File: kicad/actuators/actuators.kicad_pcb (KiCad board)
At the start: 2 copper layers, 47 parts, among them J1 Conn_01x06, J2 Conn_01x06, J3 Conn_01x06, J4 Conn_01x06, U1 DRV8874PWPR, U2 DRV8874PWPR, U3 DRV8874PWPR, U4 DRV8874PWPR, U6 STM32G431R6Tx

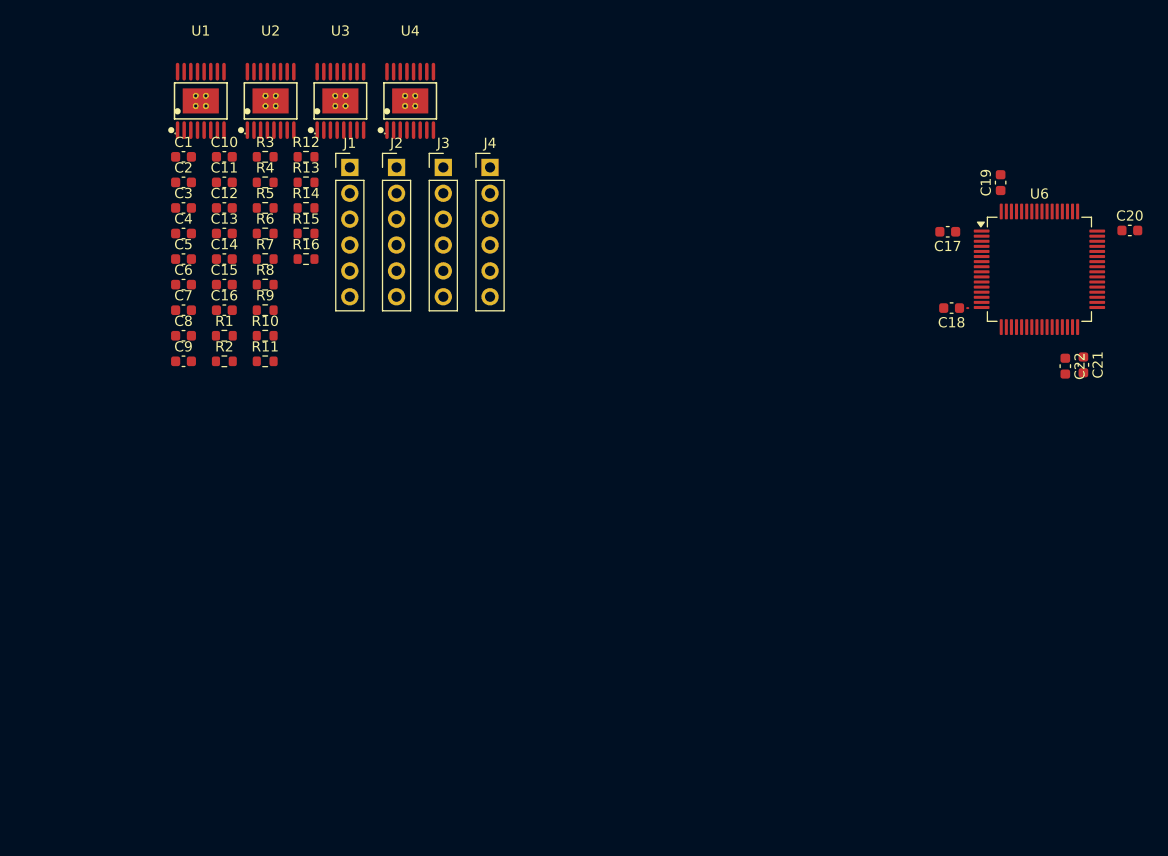
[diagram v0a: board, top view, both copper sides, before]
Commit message: completed the actuator pcb
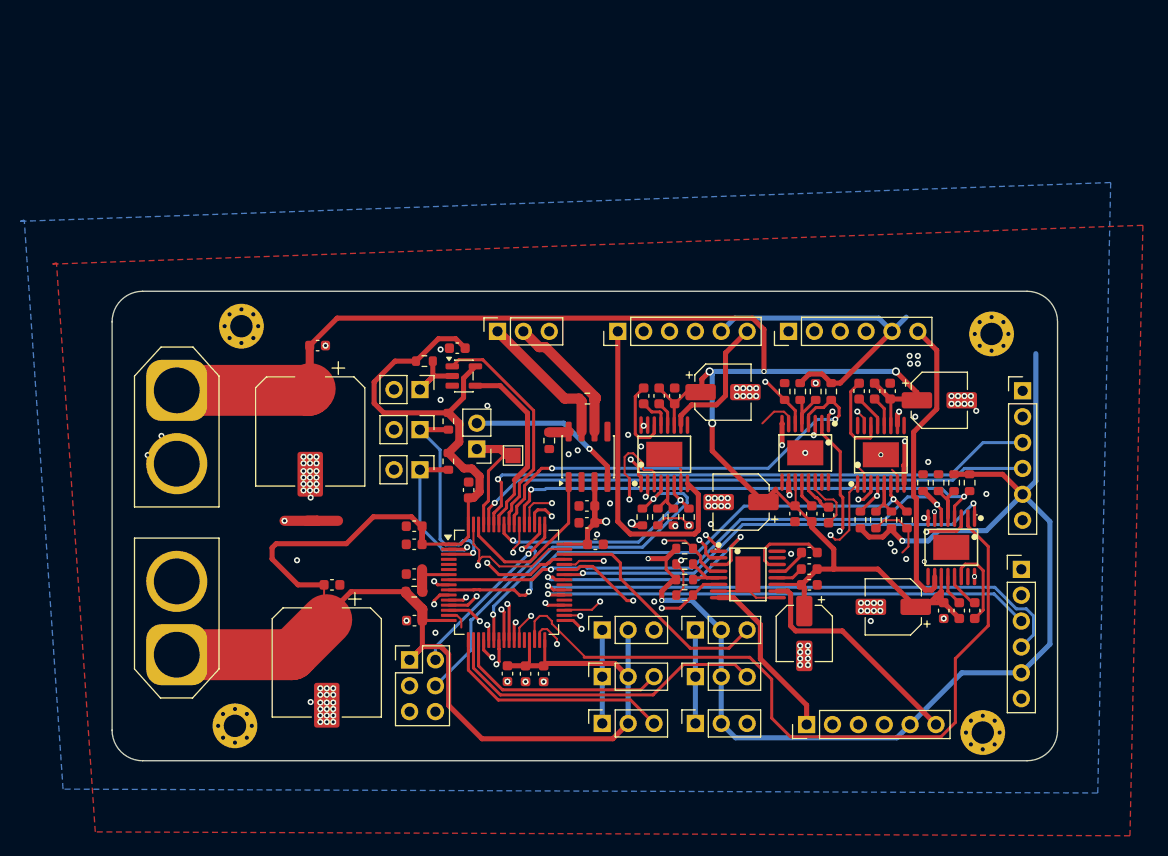
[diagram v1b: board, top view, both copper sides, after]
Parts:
- added C23: 22nF, Capacitor_SMD:C_0603_1608Metric, F.Cu at (161.6, 118.0)
- added C24: 100nf, Capacitor_SMD:C_0603_1608Metric, F.Cu at (163.1, 118.0)
- added C25: 0.1uF, Capacitor_SMD:C_0603_1608Metric, F.Cu at (169.9, 139.6)
- added C26: 100nf, Capacitor_SMD:C_0603_1608Metric, F.Cu at (164.7, 118.0)
- added C27: 22uF, Capacitor_SMD:CP_Elec_5x5.3, F.Cu at (165.0, 139.2)
- added C28: 22uF, Capacitor_SMD:CP_Elec_5x5.3, F.Cu at (169.5, 118.9)
- added C29: 22nF, Capacitor_SMD:C_0603_1608Metric, F.Cu at (156.7, 133.9)
- added C30: 100nf, Capacitor_SMD:C_0603_1608Metric, F.Cu at (156.7, 135.5)
- added C31: 22nF, Capacitor_SMD:C_0603_1608Metric, F.Cu at (158.6, 130.2)
- added C32: 100nf, Capacitor_SMD:C_0603_1608Metric, F.Cu at (157.0, 130.0)
- added C33: 0.1uF, Capacitor_SMD:C_0603_1608Metric, F.Cu at (156.7, 137.0)
- added C34: 0.1uF, Capacitor_SMD:C_0603_1608Metric, F.Cu at (155.3, 130.0)
- added C35: 22uF, Capacitor_SMD:CP_Elec_5x5.3, F.Cu at (156.2, 141.8)
- added C36: 22uF, Capacitor_SMD:CP_Elec_5x5.3, F.Cu at (150.0, 128.9)
- added J10: Conn_01x03, Connector_PinSocket_2.54mm:PinSocket_1x03_P2.54mm_Vertical, F.Cu at (136.4, 146.1)
- added J11: Conn_01x03, Connector_PinSocket_2.54mm:PinSocket_1x03_P2.54mm_Vertical, F.Cu at (136.4, 141.5)
- added J12: Conn_01x03, Connector_PinSocket_2.54mm:PinSocket_1x03_P2.54mm_Vertical, F.Cu at (126.1, 112.1)
- added J13: ESTOP SWITCH, Connector_PinHeader_2.54mm:PinHeader_1x02_P2.54mm_Vertical, F.Cu at (118.5, 117.9)
- added J14: Conn_01x06, Connector_PinHeader_2.54mm:PinHeader_1x06_P2.54mm_Vertical, F.Cu at (154.7, 112.1)
- added J15: Conn_01x06, Connector_PinHeader_2.54mm:PinHeader_1x06_P2.54mm_Vertical, F.Cu at (177.7, 118.0)
- added J16: LIMIT-SWITCH, Connector_PinHeader_2.54mm:PinHeader_1x02_P2.54mm_Vertical, F.Cu at (118.5, 125.7)
- added J17: LIMIT-SWITCH, Connector_PinHeader_2.54mm:PinHeader_1x02_P2.54mm_Vertical, F.Cu at (118.5, 121.8)
- added J18: Conn_01x06, Connector_PinHeader_2.54mm:PinHeader_1x06_P2.54mm_Vertical, F.Cu at (156.5, 150.7)
- added J19: Conn_01x06, Connector_PinHeader_2.54mm:PinHeader_1x06_P2.54mm_Vertical, F.Cu at (177.5, 135.5)
- added J5: Conn_01x06, Connector_PinHeader_2.54mm:PinHeader_1x06_P2.54mm_Vertical, F.Cu at (137.9, 112.1)
- added J6: Conn_01x03, Connector_PinSocket_2.54mm:PinSocket_1x03_P2.54mm_Vertical, F.Cu at (145.5, 150.6)
- added J7: Conn_01x03, Connector_PinSocket_2.54mm:PinSocket_1x03_P2.54mm_Vertical, F.Cu at (145.5, 146.1)
- added J8: Conn_01x03, Connector_PinSocket_2.54mm:PinSocket_1x03_P2.54mm_Vertical, F.Cu at (145.5, 141.5)
- added J9: Conn_01x03, Connector_PinSocket_2.54mm:PinSocket_1x03_P2.54mm_Vertical, F.Cu at (136.4, 150.6)
- added R17: 10k, Resistor_SMD:R_0603_1608Metric, F.Cu at (121.3, 124.9)
- added R18: 3.3k, Resistor_SMD:R_0603_1608Metric, F.Cu at (144.5, 136.5)
- added R19: 10k, Resistor_SMD:R_0603_1608Metric, F.Cu at (144.5, 135.0)
- added R20: 3.3k, Resistor_SMD:R_0603_1608Metric, F.Cu at (155.8, 118.0)
- added R21: 10k, Resistor_SMD:R_0603_1608Metric, F.Cu at (157.4, 118.0)
- added R22: 10k, Resistor_SMD:R_0603_1608Metric, F.Cu at (121.3, 121.0)
- added R23: 10k, Resistor_SMD:R_0603_1608Metric, F.Cu at (144.5, 133.5)
- added R24: 1.8k, Resistor_SMD:R_0603_1608Metric, F.Cu at (144.5, 138.0)
- added R25: 10k, Resistor_SMD:R_0603_1608Metric, F.Cu at (158.9, 118.0)
- added R26: 1.8k, Resistor_SMD:R_0603_1608Metric, F.Cu at (154.3, 118.0)
- added REF**: MountingHole_2.2mm_M2_Pad_Via, MountingHole:MountingHole_2.2mm_M2_Pad_Via, F.Cu at (173.8, 151.5)
- added REF**: MountingHole_2.2mm_M2_Pad_Via, MountingHole:MountingHole_2.2mm_M2_Pad_Via, F.Cu at (174.6, 112.4)
- added REF**: MountingHole_2.2mm_M2_Pad_Via, MountingHole:MountingHole_2.2mm_M2_Pad_Via, F.Cu at (100.3, 150.9)
- added REF**: MountingHole_2.2mm_M2_Pad_Via, MountingHole:MountingHole_2.2mm_M2_Pad_Via, F.Cu at (101.0, 111.6)
- added TP1: Boot, TestPoint:TestPoint_Pad_1.5x1.5mm, F.Cu at (127.6, 124.3)
- added U5: DRV8874PWPR, drv8874:HTSSOP-16_L5.0-W4.4-P0.65-LS6.4-BL-EP, F.Cu at (163.8, 124.3)
- added U7: DRV8874PWPR, drv8874:HTSSOP-16_L5.0-W4.4-P0.65-LS6.4-BL-EP, F.Cu at (150.7, 136.0)
- added U8: DRV8874PWPR, drv8874:HTSSOP-16_L5.0-W4.4-P0.65-LS6.4-BL-EP, F.Cu at (156.3, 124.1)
- C1: value 0.022uF -> 100nF
- C10, C11, C15, C6, C7: value 0.1uF -> 100nf
- C12: value 22uF -> 1uF
- C13: value 0.022uF -> 4.7uF
- C14: value 0.1uF -> 4.7uF
- C16: value 22uF -> 0.022uF
- C17, C18: value C -> 0.1uF
- C19: value C -> 22uF; footprint Capacitor_SMD:C_0603_1608Metric -> Capacitor_SMD:CP_Elec_5x5.3
- C2, C3: value 0.1uF -> 100nF
- C20, C22: value C -> 100nf
- C21: value C -> 22nF
- C4: value 22uF -> 470uf; footprint Capacitor_SMD:C_0603_1608Metric -> Capacitor_SMD:CP_Elec_10x10.5
- C5: value 0.022uF -> 470uf; footprint Capacitor_SMD:C_0603_1608Metric -> Capacitor_SMD:CP_Elec_10x10.5
- C8: value 22uF -> 100nf
- C9: value 0.022uF -> 100nf
- J1: value Conn_01x06 -> 3V3_IN; footprint Connector_PinHeader_2.54mm:PinHeader_1x06_P2.54mm_Vertical -> Connector_AMASS:AMASS_XT60-M_1x02_P7.20mm_Vertical
- J2: value Conn_01x06 -> 6V_IN; footprint Connector_PinHeader_2.54mm:PinHeader_1x06_P2.54mm_Vertical -> Connector_AMASS:AMASS_XT60-M_1x02_P7.20mm_Vertical
- J3: value Conn_01x06 -> Jumper; footprint Connector_PinHeader_2.54mm:PinHeader_1x06_P2.54mm_Vertical -> Connector_PinHeader_2.54mm:PinHeader_1x02_P2.54mm_Vertical
- J4: value Conn_01x06 -> Conn_02x03_Odd_Even; footprint Connector_PinHeader_2.54mm:PinHeader_1x06_P2.54mm_Vertical -> Connector_PinHeader_2.54mm:PinHeader_2x03_P2.54mm_Vertical
- R10: value 10k -> 3.3k
- R12: value 1.8k -> 10k
- R13, R3, R9: value 3.3k -> 10k
- R14: value 10k -> 1.8k
- R2, R8: value 1.8k -> 3.3k
- R5: value 3.3k -> 1.8k
- R7: value 10k -> 120
- U1: value DRV8874PWPR -> STM32G431R6Tx; footprint drv8874:HTSSOP-16_L5.0-W4.4-P0.65-LS6.4-BL-EP -> Package_QFP:LQFP-64_10x10mm_P0.5mm
- U3: value DRV8874PWPR -> SN65HVD230; footprint drv8874:HTSSOP-16_L5.0-W4.4-P0.65-LS6.4-BL-EP -> Package_SO:SOIC-8_3.9x4.9mm_P1.27mm
- U6: value STM32G431R6Tx -> 74LVC1G08; footprint Package_QFP:LQFP-64_10x10mm_P0.5mm -> Package_TO_SOT_SMD:SOT-23-5
- moved R13 71.5 mm to (172.5, 127.0), turned to -90 degrees
- moved R8 70.4 mm to (170.9, 127.0), turned to -90 degrees
- moved U4 68.9 mm to (170.7, 133.3), turned to 180 degrees
- moved R9 68.3 mm to (169.4, 127.0), turned to 90 degrees
- moved C20 67.0 mm to (122.2, 113.8)
- moved R14 66.3 mm to (167.9, 127.0), turned to 90 degrees
- moved R16 64.3 mm to (166.3, 130.7), turned to -90 degrees
- moved R10 64.1 mm to (164.8, 130.7), turned to 90 degrees
- moved R11 62.0 mm to (163.3, 130.7), turned to -90 degrees
- moved R15 61.3 mm to (161.7, 130.7), turned to 90 degrees
- moved U6 57.5 mm to (122.8, 116.5)
- moved U1 56.0 mm to (127.0, 136.8)
- moved R3 52.3 mm to (141.9, 130.4), turned to -90 degrees
- moved U2 51.9 mm to (142.5, 124.2)
- moved R5 51.5 mm to (144.9, 130.4), turned to -90 degrees
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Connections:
- C1 pad 1: Net-(U1-CPL) -> Net-(U1-PG10)
- C1 pad 2: Net-(U1-CPH) -> GND
- C10 pad 1: Net-(U3-VCP) -> +3V3
- C10 pad 2: +6V -> GND
- C11 pad 1: +6V -> +3V3
- C12 pad 1: +6V -> +3V3
- C13 pad 1: Net-(U4-CPL) -> +3V3
- C13 pad 2: Net-(U4-CPH) -> GND
- C14 pad 1: Net-(U4-VCP) -> +3V3
- C14 pad 2: +6V -> GND
- C15 pad 1: +6V -> +3V3
- C16 pad 1: +6V -> Net-(U2-CPL)
- C16 pad 2: GND -> Net-(U2-CPH)
- C17 pad 1: Net-(U6-VBAT) -> Net-(U2-VCP)
- C17 pad 2: GND -> +6V
- C18 pad 1: Net-(U6-VBAT) -> +6V
- C19 pad 1: Net-(U6-VBAT) -> +6V
- C2 pad 1: Net-(U1-VCP) -> +3V3
- C2 pad 2: +6V -> GND
- C20 pad 1: Net-(U6-VBAT) -> GND
- C20 pad 2: GND -> +3V3
- C21 pad 1: Net-(U6-VBAT) -> Net-(U4-CPL)
- C21 pad 2: GND -> Net-(U4-CPH)
- C22 pad 1: Net-(U6-VBAT) -> Net-(U4-VCP)
- C22 pad 2: GND -> +6V
- C4 pad 1: +6V -> +3V3
- C5 pad 1: Net-(U2-CPL) -> +6V
- C5 pad 2: Net-(U2-CPH) -> GND
- C6 pad 1: Net-(U2-VCP) -> +3V3
- C6 pad 2: +6V -> GND
- C7 pad 1: +6V -> +3V3
- C8 pad 1: +6V -> +3V3
- C9 pad 1: Net-(U3-CPL) -> +3V3
- C9 pad 2: Net-(U3-CPH) -> GND
- J1 pad 1: /DRV8874PWPR/M1A -> +3V3
- J2 pad 1: /DRV8874PWPR/M2A -> +6V
- J3 pad 1: /DRV8874PWPR/M3A -> Net-(J3-Pin_1)
- J3 pad 2: GND -> /CAN-R
- J4 pad 1: /DRV8874PWPR/M4A -> +3V3
- J4 pad 2: GND -> /SWDIO
- J4 pad 3: /DRV8874PWPR/E4A -> GND
- J4 pad 4: /DRV8874PWPR/E4B -> /SWCLK
- J4 pad 5: +3V3 -> /NRST
- J4 pad 6: /DRV8874PWPR/M4B -> GND
- R1 pad 2: /DRV8874PWPR/M1_FAULT -> Net-(U1-PG10)
- R10 pad 1: Net-(U3-VREF) -> +3V3
- R10 pad 2: GND -> Net-(U5-VREF)
- R11 pad 1: +3V3 -> Net-(U5-VREF)
- R11 pad 2: /DRV8874PWPR/M1_FAULT -> GND
- R12 pad 1: /DRV8874PWPR/M1_ADC -> Net-(J13-Pin_1)
- R12 pad 2: GND -> +3V3
- R13 pad 2: Net-(U4-VREF) -> /M2_FAULT
- R14 pad 1: Net-(U4-VREF) -> /M1_ADC
- R15 pad 2: /DRV8874PWPR/M1_FAULT -> /M3_FAULT
- R16 pad 1: /DRV8874PWPR/M1_ADC -> /M3_ADC
- R2 pad 1: /DRV8874PWPR/M1_ADC -> +3V3
- R2 pad 2: GND -> Net-(U2-VREF)
- R3 pad 1: +3V3 -> Net-(U2-VREF)
- R3 pad 2: Net-(U1-VREF) -> GND
- R4 pad 1: Net-(U1-VREF) -> +3V3
- R4 pad 2: GND -> /M5_FAULT
- R5 pad 1: +3V3 -> /M5_ADC
- R5 pad 2: Net-(U2-VREF) -> GND
- R6 pad 1: Net-(U2-VREF) -> GND
- R6 pad 2: GND -> Net-(U3-Rs)
- R7 pad 1: +3V3 -> Net-(J12-Pin_2)
- R7 pad 2: /DRV8874PWPR/M1_FAULT -> Net-(J12-Pin_1)
- R8 pad 1: /DRV8874PWPR/M1_ADC -> +3V3
- R8 pad 2: GND -> Net-(U4-VREF)
- R9 pad 1: +3V3 -> Net-(U4-VREF)
- R9 pad 2: Net-(U3-VREF) -> GND
- U1 pad 1: /DRV8874PWPR/M1_PWM -> +3V3
- U1 pad 10: /DRV8874PWPR/M1B -> /M3_ADC
- U1 pad 11: +6V -> /M4_ADC
- U1 pad 12: Net-(U1-VCP) -> /E1A
- U1 pad 13: Net-(U1-CPH) -> /E1B
- U1 pad 14: Net-(U1-CPL) -> /SR1
- U1 pad 16: GND -> +3V3
- U1 pad 17: GND -> /SR2
- U1 pad 2: /DRV8874PWPR/M1_DIR -> /TOPL
- U1 pad 3: /DRV8874PWPR/M1_ENA -> /BOML
- U1 pad 4: /DRV8874PWPR/M1_FAULT -> unconnected-(U1-PC15-Pad4)
- U1 pad 5: Net-(U1-VREF) -> unconnected-(U1-PF0-Pad5)
- U1 pad 6: /DRV8874PWPR/M1_ADC -> unconnected-(U1-PF1-Pad6)
- U1 pad 7: GND -> Net-(U1-PG10)
- U1 pad 8: /DRV8874PWPR/M1A -> /M1_ADC
- U1 pad 9: GND -> /M2_ADC
- U2 pad 1: /DRV8874PWPR/M1_PWM -> /M5_PWM
- U2 pad 10: /DRV8874PWPR/M2B -> /M5B
- U2 pad 2: /DRV8874PWPR/M1_DIR -> /M5_DIR
- U2 pad 3: /DRV8874PWPR/M1_ENA -> /M5_ENA
- U2 pad 4: /DRV8874PWPR/M1_FAULT -> /M5_FAULT
- U2 pad 6: /DRV8874PWPR/M1_ADC -> /M5_ADC
- U2 pad 8: /DRV8874PWPR/M2A -> /M5A
- U3 pad 1: /DRV8874PWPR/M1_PWM -> /CAN-D
- U3 pad 2: /DRV8874PWPR/M1_DIR -> GND
- U3 pad 3: /DRV8874PWPR/M1_ENA -> +3V3
- U3 pad 4: /DRV8874PWPR/M1_FAULT -> /CAN-R
- U3 pad 5: Net-(U3-VREF) -> unconnected-(U3-Vref-Pad5)
- U3 pad 6: /DRV8874PWPR/M1_ADC -> Net-(J12-Pin_2)
- U3 pad 7: GND -> Net-(J12-Pin_1)
- U3 pad 8: /DRV8874PWPR/M3A -> Net-(U3-Rs)
- U4 pad 1: /DRV8874PWPR/M1_PWM -> /M1_PWM
- U4 pad 10: /DRV8874PWPR/M4B -> /Wheels/M1B
- U4 pad 2: /DRV8874PWPR/M1_DIR -> /M1_DIR
- U4 pad 3: /DRV8874PWPR/M1_ENA -> /nSLEEP
- U4 pad 4: /DRV8874PWPR/M1_FAULT -> /M2_FAULT
- U4 pad 6: /DRV8874PWPR/M1_ADC -> /M1_ADC
- U4 pad 8: /DRV8874PWPR/M4A -> /Wheels/M1A
- U6 pad 1: Net-(U6-VBAT) -> /MOTOR_RUN
- U6 pad 2: unconnected-(U6-PC13-Pad2) -> Net-(J13-Pin_1)
- U6 pad 3: unconnected-(U6-PC14-Pad3) -> GND
- U6 pad 4: unconnected-(U6-PC15-Pad4) -> /MOTOR_EN
- U6 pad 5: unconnected-(U6-PF0-Pad5) -> +3V3
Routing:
- net +3V3: track 0.00 -> 366.5 mm, vias 0 -> 6
- net +6V: track 0.00 -> 164.9 mm, vias 0 -> 4
- net GND: track 0.00 -> 86.9 mm, vias 0 -> 125
- net /M1_DIR: track 0.00 -> 74.5 mm
- net /nSLEEP: track 0.00 -> 67.4 mm, vias 0 -> 5
- net /E1A: track 0.00 -> 61.9 mm, vias 0 -> 1
- net /E1B: track 0.00 -> 59.1 mm, vias 0 -> 1
- net /E3A: track 0.00 -> 57.9 mm, vias 0 -> 1
- net /M1_ADC: track 0.00 -> 57.1 mm, vias 0 -> 2
- net /E3B: track 0.00 -> 55.6 mm, vias 0 -> 1
- net /E4B: track 0.00 -> 54.2 mm, vias 0 -> 1
- net /M3_ADC: track 0.00 -> 53.5 mm, vias 0 -> 2
- net /M4_ADC: track 0.00 -> 52.6 mm, vias 0 -> 2
- net /M4_PWM: track 0.00 -> 50.4 mm, vias 0 -> 2
- net /M2_FAULT: track 0.00 -> 50.3 mm, vias 0 -> 2
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- added copper zone on B.Cu, net +3V3
- added copper zone on In1.Cu, net +6V
- added copper zone on F.Cu, net GND
- added copper zone on In2.Cu, net GND
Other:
- board outline added: 92.8 x 46.1 mm
- copper layers 2 -> 4

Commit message: formatted some files
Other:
- board text added: "3V3"
- board text added: "6V"
- board text added: "BOML"
- board text added: "CLK"
- board text added: "DIO"
- board text added: "ESTOP SW"
- board text added: "GND"
- board text added: "RST"
- board text added: "S1"
- board text added: "S2"
- board text added: "S3"
- board text added: "S4"
- board text added: "S5"
- board text added: "S6"
- board text added: "TOPL"

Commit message: updated the radio board and changed the servo headers to 6v from 3v3
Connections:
- J10 pad 2: +3V3 -> +6V
- J11 pad 2: +3V3 -> +6V
- J6 pad 2: +3V3 -> +6V
- J7 pad 2: +3V3 -> +6V
- J8 pad 2: +3V3 -> +6V
- J9 pad 2: +3V3 -> +6V
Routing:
- net +3V3: track 366.5 -> 295.5 mm, vias 6 -> 7
- net +6V: track 164.9 -> 175.2 mm

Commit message: completed the radio board, and making power board
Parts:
- removed the REF** at (100.3, 150.9)
- added C37: 100nF, Capacitor_SMD:C_0603_1608Metric, F.Cu at (103.8, 140.3)
- added C38: 470uf, Capacitor_SMD:CP_Elec_10x10.5, F.Cu at (107.6, 147.0)
- added J20: 6V2_IN, Connector_AMASS:AMASS_XT30U-M_1x02_P5.0mm_Vertical, F.Cu at (94.5, 143.6)
- J1, J2: footprint Connector_AMASS:AMASS_XT60-M_1x02_P7.20mm_Vertical -> Connector_AMASS:AMASS_XT30U-M_1x02_P5.0mm_Vertical
- moved C2 12.3 mm to (103.3, 126.6), turned to 180 degrees
- moved C4 11.6 mm to (107.5, 133.2)
- moved J1 9.94 mm to (94.5, 133.9)
- moved J2 3.76 mm to (94.6, 114.2)
- moved C5 2.71 mm to (107.2, 119.3)
- moved C3 2.33 mm to (107.7, 111.3)
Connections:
- J10 pad 2: +6V -> +6V2
- J11 pad 2: +6V -> +6V2
- J6 pad 2: +6V -> +6V2
- J7 pad 2: +6V -> +6V2
- J8 pad 2: +6V -> +6V2
- J9 pad 2: +6V -> +6V2
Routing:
- net +6V2: track 0.00 -> 144.1 mm, vias 0 -> 18
- net +3V3: track 295.5 -> 393.2 mm, vias 7 -> 8
- net GND: track 86.9 -> 65.0 mm, vias 125 -> 135
- net +6V: track 175.2 -> 171.7 mm, vias 4 -> 22
- net Net-(U8-CPL): track 6.40 -> 4.94 mm
- net /M5A: track 32.9 -> 32.3 mm
- net /M5_PWM: track 22.5 -> 21.9 mm
- added copper zone on B.Cu, net +6V2
- removed copper zone on B.Cu, net +3V3
